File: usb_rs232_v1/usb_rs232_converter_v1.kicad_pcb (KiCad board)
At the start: 2 copper layers, 39.4 x 59.7 mm, 5 parts, among them CON1 USB-MINI-B, CON2 USB-MICRO-B, J1 DB9, J2 DB9

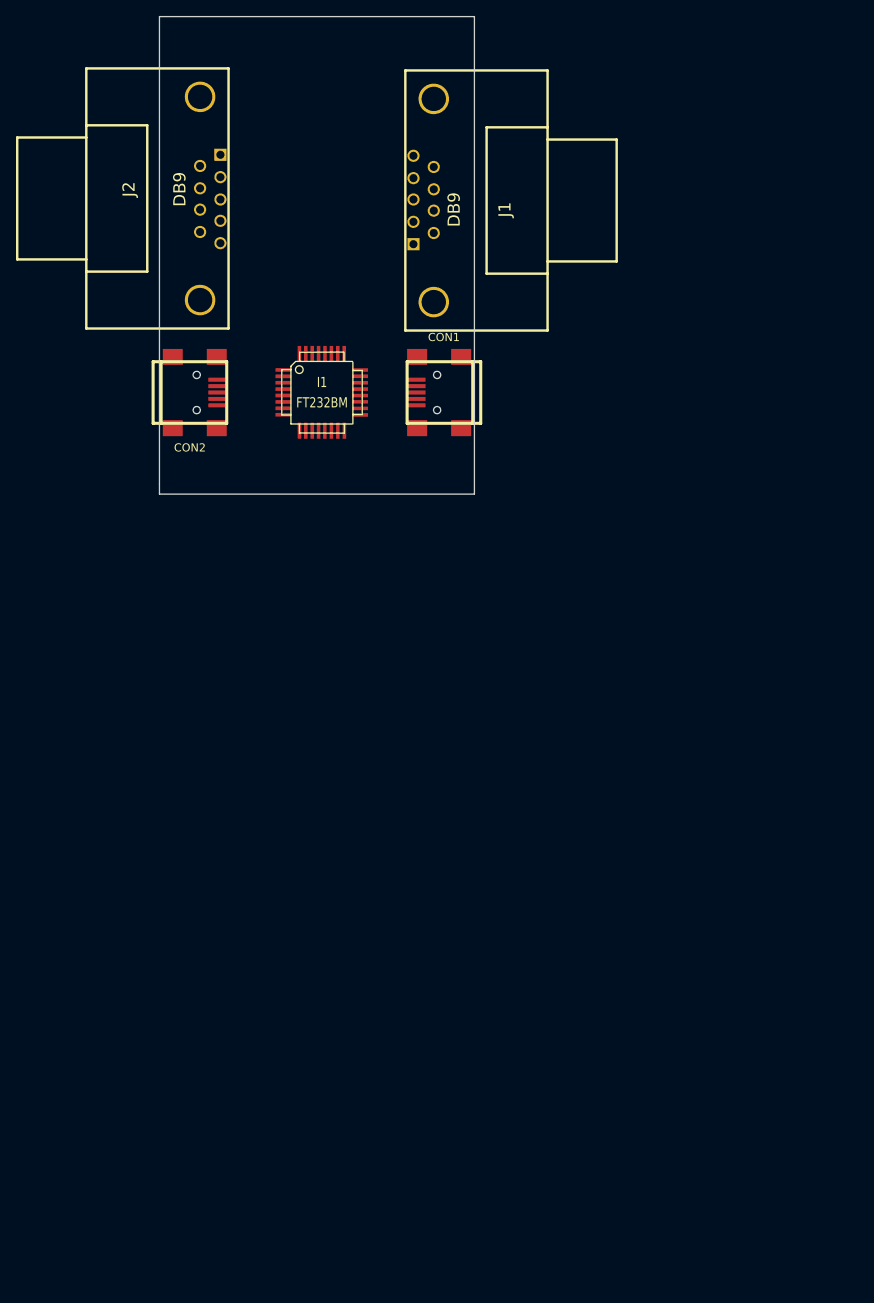
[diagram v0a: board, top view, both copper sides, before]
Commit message: Dodane biblioteki z sieci
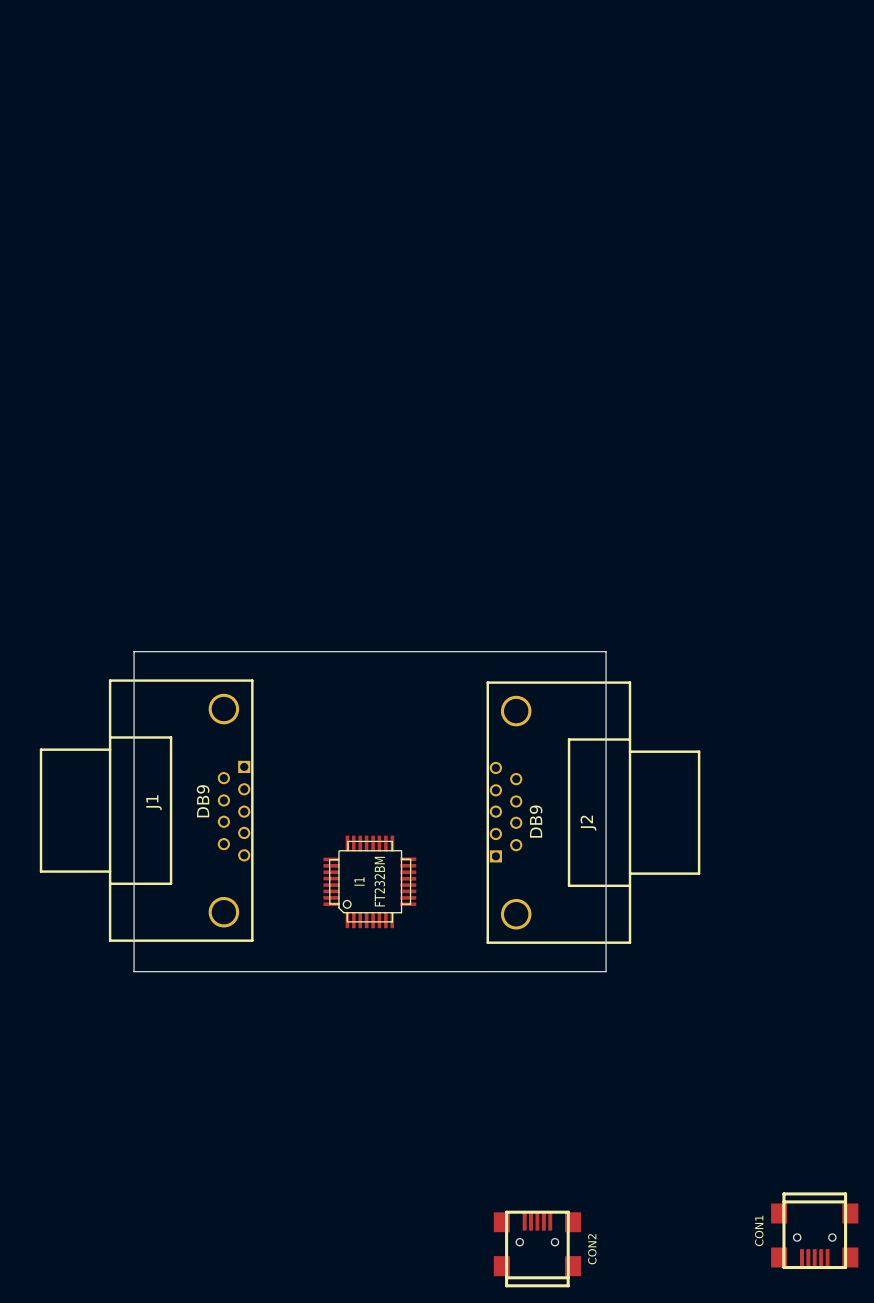
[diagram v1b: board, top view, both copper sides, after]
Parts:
- moved CON2 115.5 mm to (159.0, 235.3), turned to 90 degrees
- moved CON1 114.6 mm to (193.7, 233.0), turned to 270 degrees
- moved J2 85.0 mm to (155.1, 180.7), turned to 270 degrees
- moved J1 80.1 mm to (121.1, 180.7), turned to 90 degrees
- moved I1 61.4 mm to (138.1, 189.4), turned to 90 degrees
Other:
- board size 39.4 x 59.7 mm -> 59 x 40 mm
- net class pwr added: clearance 0.6096, trace_width 0.6096, via_dia 1.3, via_drill 0.9
- board text added: "siatki: - 0,508 elementy"
